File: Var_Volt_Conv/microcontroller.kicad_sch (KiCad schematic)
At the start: 7 parts

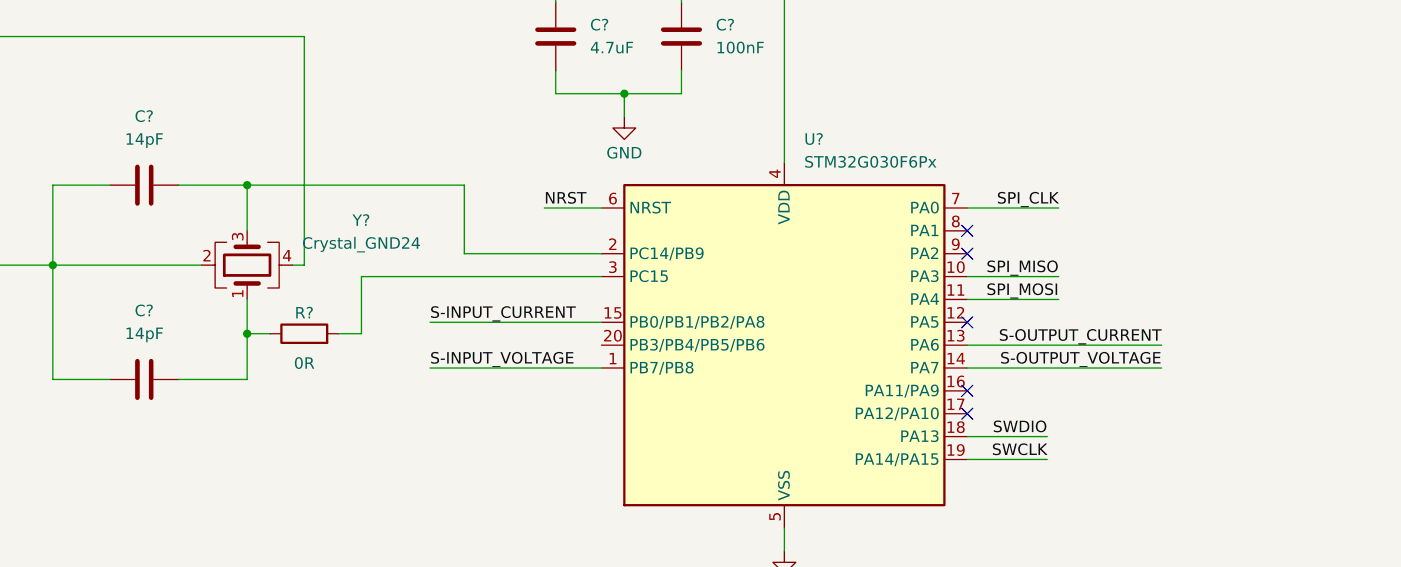
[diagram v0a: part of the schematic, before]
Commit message: Changed all labels to flags, except for NRST, SWDIO and SWCLK
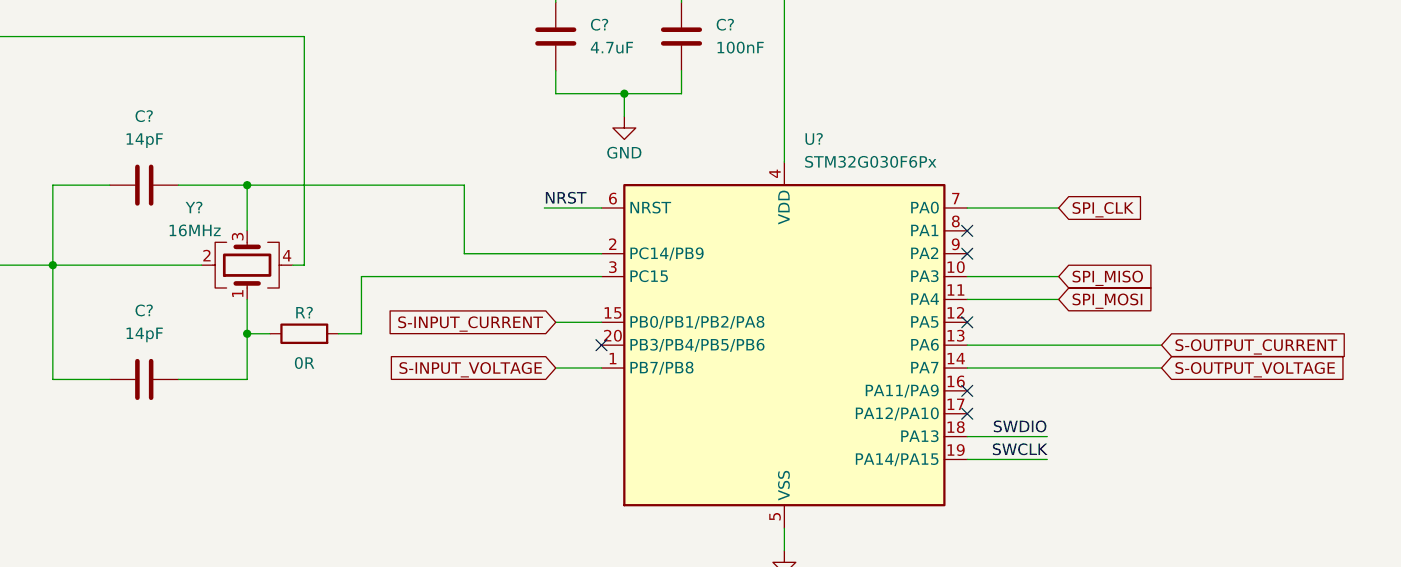
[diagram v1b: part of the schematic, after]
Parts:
- Y?: value Crystal_GND24 -> 16MHz
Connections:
- no-connect marks 5 -> 6
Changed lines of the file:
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@@
+	)
+	(no_connect
+		(at 114.3 86.36)
 	)
 	(no_connect
@@
 	(wire
 		(pts
-			(xy 95.25 88.9) (xy 114.3 88.9)
+			(xy 109.22 88.9) (xy 114.3 88.9)
 		)
 		(stroke
@@
 	(wire
 		(pts
-			(xy 95.25 83.82) (xy 114.3 83.82)
+			(xy 109.22 83.82) (xy 114.3 83.82)
 		)
 		(stroke
@@
 			(width 0)
 			(type default)
-		)
-	)
-	(label "S-INPUT_CURRENT"
-		(at 95.25 83.82 0)
-		(fields_autoplaced yes)
-		(effects
-			(font
-				(size 1.27 1.27)
-			)
-			(justify left bottom)
 		)
 	)
@@
 		)
 	)
-	(label "SPI_CLK"
-		(at 165.1 71.12 180)
-		(fields_autoplaced yes)
-		(effects
-			(font
-				(size 1.27 1.27)
-			)
-			(justify right bottom)
-		)
-	)
 	(label "SWDIO"
 		(at 163.83 96.52 180)
@@
 		)
 	)
-	(label "S-INPUT_VOLTAGE"
-		(at 95.25 88.9 0)
-		(fields_autoplaced yes)
-		(effects
-			(font
-				(size 1.27 1.27)
-			)
-			(justify left bottom)
-		)
-	)
-	(label "S-OUTPUT_CURRENT"
-		(at 176.53 86.36 180)
-		(fields_autoplaced yes)
-		(effects
-			(font
-				(size 1.27 1.27)
-			)
-			(justify right bottom)
-		)
-	)
-	(label "S-OUTPUT_VOLTAGE"
-		(at 176.53 88.9 180)
-		(fields_autoplaced yes)
-		(effects
-			(font
-				(size 1.27 1.27)
-			)
-			(justify right bottom)
-		)
-	)
-	(label "SPI_MISO"
-		(at 165.1 78.74 180)
-		(fields_autoplaced yes)
-		(effects
-			(font
-				(size 1.27 1.27)
-			)
-			(justify right bottom)
-		)
-	)
 	(label "SWCLK"
 		(at 163.83 99.06 180)
@@
 		)
 	)
-	(label "SPI_MOSI"
-		(at 165.1 81.28 180)
-		(fields_autoplaced yes)
-		(effects
-			(font
-				(size 1.27 1.27)
-			)
-			(justify right bottom)
+	(global_label "SPI_MOSI"
+		(shape input)
+		(at 165.1 81.28 0)
+		(fields_autoplaced yes)
+		(effects
+			(font
+				(size 1.27 1.27)
+			)
+			(justify left)
+		)
+		(property "Intersheetrefs" "${INTERSHEET_REFS}"
+			(at 176.7333 81.28 0)
+			(effects
+				(font
+					(size 1.27 1.27)
+				)
+				(justify left)
+				(hide yes)
+			)
+		)
+	)
+	(global_label "SPI_CLK"
+		(shape input)
+		(at 165.1 71.12 0)
+		(fields_autoplaced yes)
+		(effects
+			(font
+				(size 1.27 1.27)
+			)
+			(justify left)
+		)
+		(property "Intersheetrefs" "${INTERSHEET_REFS}"
+			(at 175.7052 71.12 0)
+			(effects
+				(font
+					(size 1.27 1.27)
+				)
+				(justify left)
+				(hide yes)
+			)
+		)
+	)
+	(global_label "S-OUTPUT_VOLTAGE"
+		(shape input)
+		(at 176.53 88.9 0)
+		(fields_autoplaced yes)
+		(effects
+			(font
+				(size 1.27 1.27)
+			)
+			(justify left)
+		)
+		(property "Intersheetrefs" "${INTERSHEET_REFS}"
+			(at 198.3838 88.9 0)
+			(effects
+				(font
+					(size 1.27 1.27)
+				)
+				(justify left)
+				(hide yes)
+			)
+		)
+	)
+	(global_label "S-OUTPUT_CURRENT"
+		(shape input)
+		(at 176.53 86.36 0)
+		(fields_autoplaced yes)
+		(effects
+			(font
+				(size 1.27 1.27)
+			)
+			(justify left)
+		)
+		(property "Intersheetrefs" "${INTERSHEET_REFS}"
+			(at 199.049 86.36 0)
+			(effects
+				(font
+					(size 1.27 1.27)
+				)
+				(justify left)
+				(hide yes)
+			)
+		)
+	)
+	(global_label "S-INPUT_VOLTAGE"
+		(shape input)
+		(at 109.22 88.9 180)
+		(fields_autoplaced yes)
+		(effects
+			(font
+				(size 1.27 1.27)
+			)
+			(justify right)
+		)
+		(property "Intersheetrefs" "${INTERSHEET_REFS}"
+			(at 89.0595 88.9 0)
+			(effects
+				(font
+					(size 1.27 1.27)
+				)
+				(justify right)
+				(hide yes)
+			)
+		)
+	)
+	(global_label "SPI_MISO"
+		(shape input)
+		(at 165.1 78.74 0)
+		(fields_autoplaced yes)
+		(effects
+			(font
+				(size 1.27 1.27)
+			)
+			(justify left)
+		)
+		(property "Intersheetrefs" "${INTERSHEET_REFS}"
+			(at 176.7333 78.74 0)
+			(effects
+				(font
+					(size 1.27 1.27)
+				)
+				(justify left)
+				(hide yes)
+			)
+		)
+	)
+	(global_label "S-INPUT_CURRENT"
+		(shape input)
+		(at 109.22 83.82 180)
+		(fields_autoplaced yes)
+		(effects
+			(font
+				(size 1.27 1.27)
+			)
+			(justify right)
+		)
+		(property "Intersheetrefs" "${INTERSHEET_REFS}"
+			(at 88.3943 83.82 0)
+			(effects
+				(font
+					(size 1.27 1.27)
+				)
+				(justify right)
+				(hide yes)
+			)
 		)
 	)
@@
 		(on_board yes)
 		(dnp no)
-		(fields_autoplaced yes)
 		(property "Reference" "Y?"
-			(at 87.63 72.5168 90)
-			(effects
-				(font
-					(size 1.27 1.27)
-				)
-			)
-		)
-		(property "Value" "Crystal_GND24"
-			(at 87.63 75.0568 90)
-			(effects
-				(font
+			(at 69.088 71.12 90)
+			(effects
+				(font
+					(size 1.27 1.27)
+				)
+			)
+		)
+		(property "Value" "16MHz"
+			(at 69.088 73.66 90)
+			(effects
+				(font

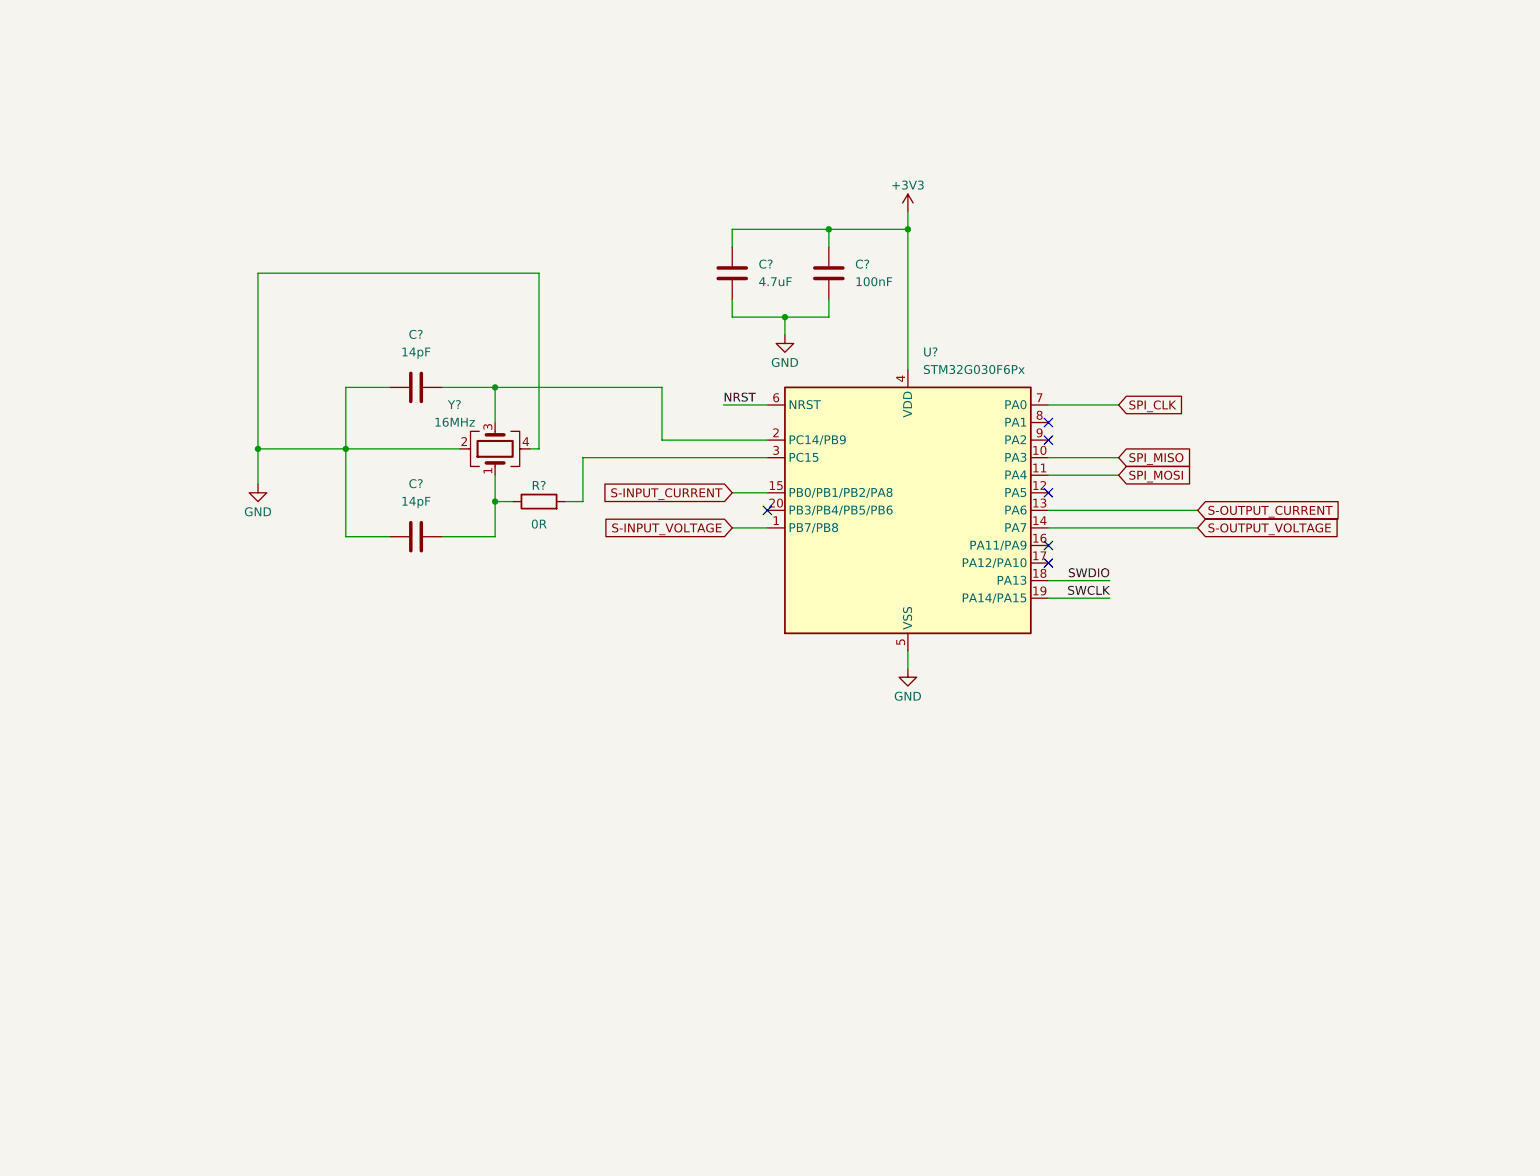
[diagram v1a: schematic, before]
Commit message: Add SWD connector
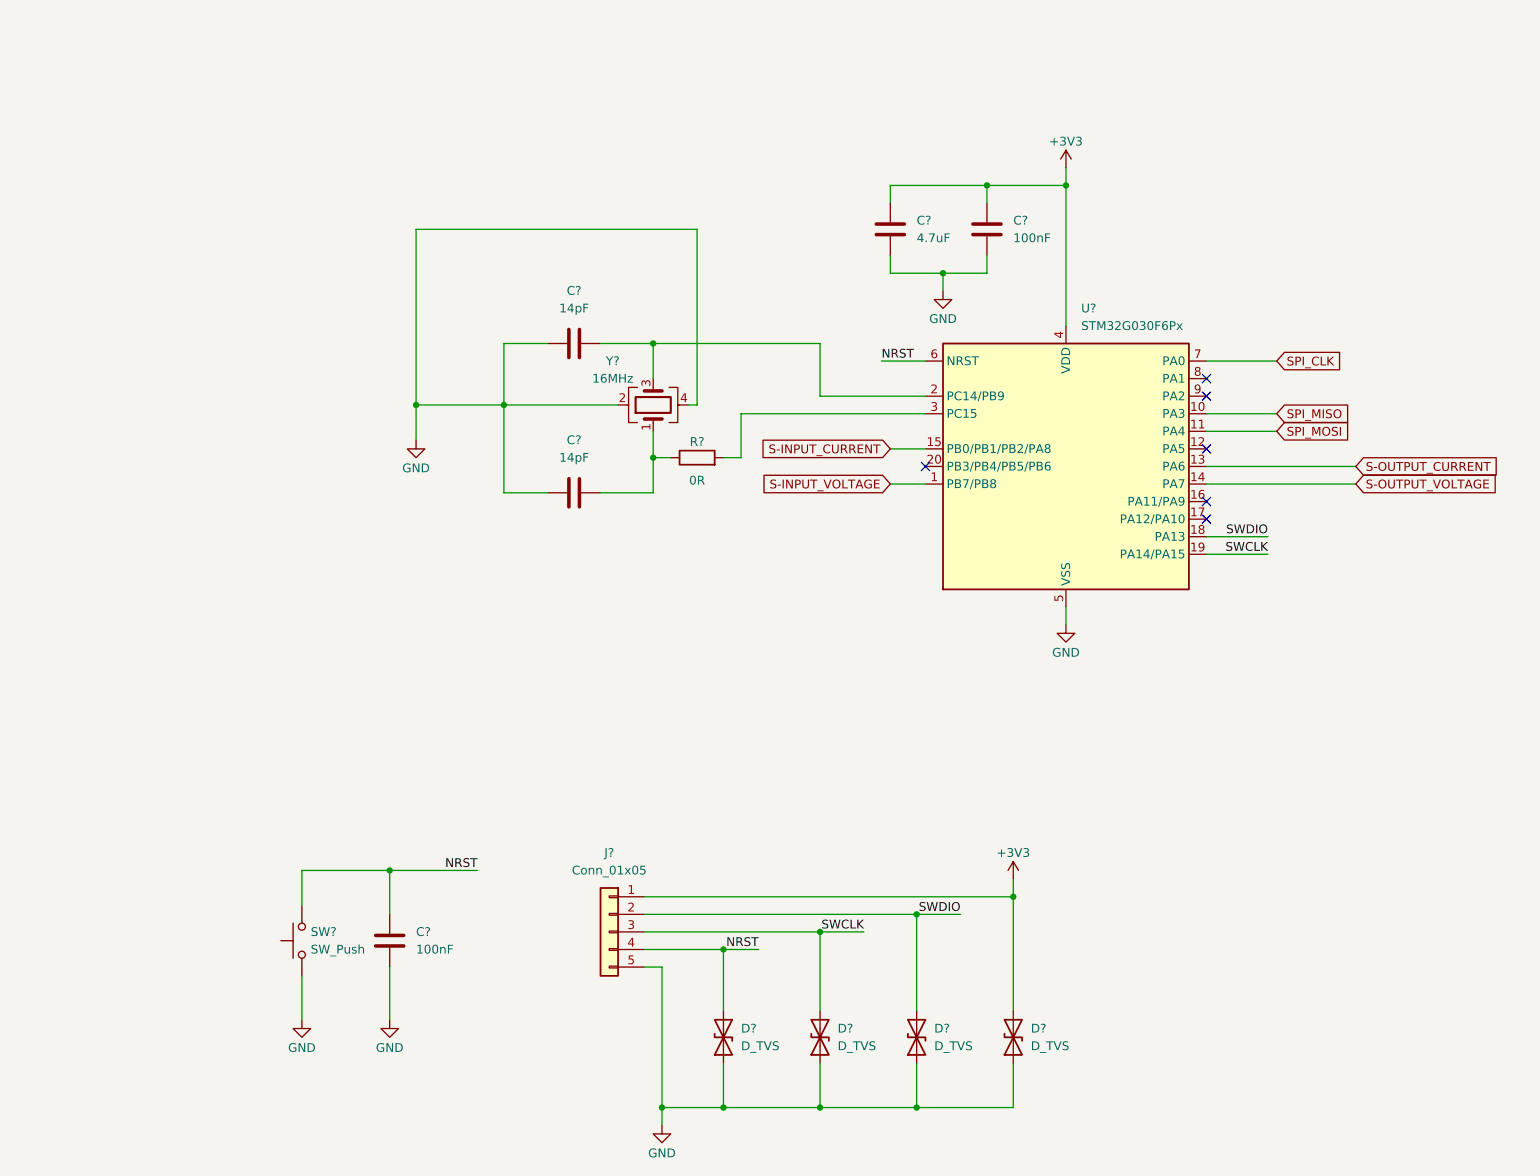
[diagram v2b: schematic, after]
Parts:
- added C?: 100nF, symbol Device:C
- added D? (x4): D_TVS, symbol Device:D_TVS
- added J?: Conn_01x05, symbol Connector_Generic:Conn_01x05
- added SW?: SW_Push, symbol Switch:SW_Push
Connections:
- net +3V3: now also D?.2 (A2), J?.1 (Pin_1)
- net GND: now also C?.2, D?.1 (A1), D?.1 (A1), D?.1 (A1), D?.1 (A1), J?.5 (Pin_5), SW?.1
- net NRST: now also C?.1, D?.2 (A2), J?.4 (Pin_4), SW?.2
- net SWCLK: now also D?.2 (A2), J?.3 (Pin_3)
- net SWDIO: now also D?.2 (A2), J?.2 (Pin_2)
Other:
- moved on the sheet: C?, R?, U?, Y?

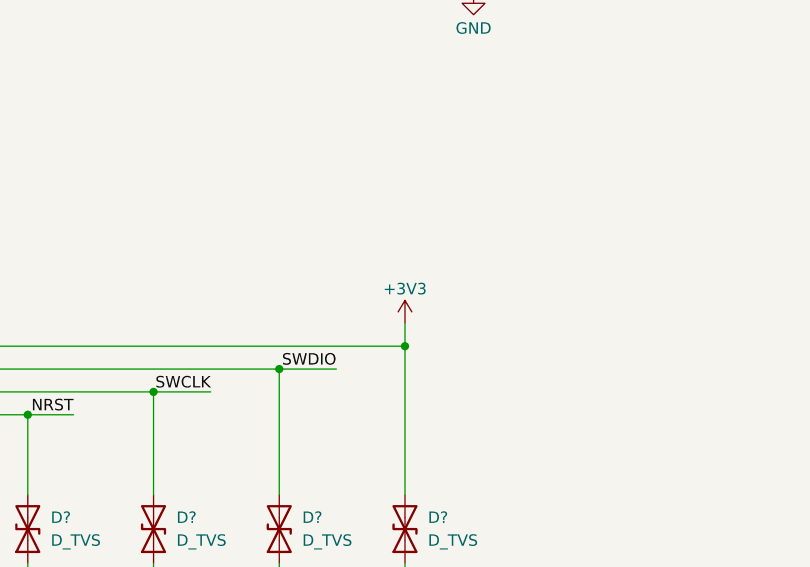
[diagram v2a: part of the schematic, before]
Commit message: Add 3.3V buck Converter TPS61272DSGT
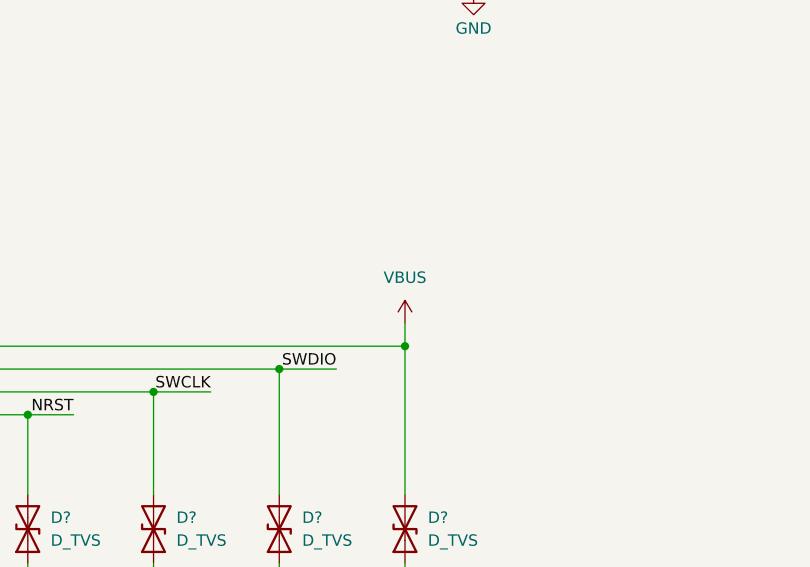
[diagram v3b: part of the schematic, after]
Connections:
- net +3V3: no longer D?.2 (A2), J?.1 (Pin_1)
- new net VBUS: D?.2 (A2), J?.1 (Pin_1)
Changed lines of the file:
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@@
+	)
+	(symbol
+		(lib_id "power:VBUS")
+		(at 149.86 139.7 0)
+		(unit 1)
+		(exclude_from_sim no)
+		(in_bom yes)
+		(on_board yes)
+		(dnp no)
+		(fields_autoplaced yes)
+		(property "Reference" "#PWR08"
+			(at 149.86 143.51 0)
+			(effects
+				(font
+					(size 1.27 1.27)
+				)
+				(hide yes)
+			)
+		)
+		(property "Value" "VBUS"
+			(at 149.86 134.62 0)
+			(effects
+				(font
+					(size 1.27 1.27)
+				)
+			)
+		)
+		(property "Footprint" ""
+			(at 149.86 139.7 0)
+			(effects
+				(font
+					(size 1.27 1.27)
+				)
+				(hide yes)
+			)
+		)
+		(property "Datasheet" ""
+			(at 149.86 139.7 0)
+			(effects
+				(font
+					(size 1.27 1.27)
+				)
+				(hide yes)
+			)
+		)
+		(property "Description" "Power symbol creates a global label with name \"VBUS\""
+			(at 149.86 139.7 0)
+			(effects
+				(font
+					(size 1.27 1.27)
+				)
+				(hide yes)
+			)
+		)
+		(pin "1"
+		)
+		(instances
+			(project ""
+				(path "/7c9580d6-c22f-4506-b9c3-9272e882c9fb/b048280b-6fef-4656-96bb-ca0a0c35ac5b"
+					(reference "#PWR08")
+					(unit 1)
+				)
+			)
+		)
 	)
 	(symbol
@@
 					(unit 1)
 				)
-			)
-		)
-	)
-	(symbol
-		(lib_id "power:+3V3")
-		(at 149.86 139.7 0)
-		(unit 1)
-		(exclude_from_sim no)
-		(in_bom yes)
-		(on_board yes)
-		(dnp no)
-		(property "Reference" "#PWR08"
-			(at 149.86 143.51 0)
-			(effects
-				(font
-					(size 1.27 1.27)
-				)
-				(hide yes)
-			)
-		)
-		(property "Value" "+3V3"
-			(at 149.86 135.89 0)
-			(effects
-				(font
-					(size 1.27 1.27)
-				)
-			)
-		)
-		(property "Footprint" ""
-			(at 149.86 139.7 0)
-			(effects
-				(font
-					(size 1.27 1.27)
-				)
-				(hide yes)
-			)
-		)
-		(property "Datasheet" ""
-			(at 149.86 139.7 0)
-			(effects
-				(font
-					(size 1.27 1.27)
-				)
-				(hide yes)
-			)
-		)
-		(property "Description" "Power symbol creates a global label with name \"+3V3\""
-			(at 149.86 139.7 0)
-			(effects
-				(font
-					(size 1.27 1.27)
-				)
-				(hide yes)
-			)
-		)
-		(pin "1"
-		)
-		(instances
-			(project "Var_Volt_Conv"
-				(path "/7c9580d6-c22f-4506-b9c3-9272e882c9fb/b048280b-6fef-4656-96bb-ca0a0c35ac5b"
-					(reference "#PWR08")
-					(unit 1)
-				)
